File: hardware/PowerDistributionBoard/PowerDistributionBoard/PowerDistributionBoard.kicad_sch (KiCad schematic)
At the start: 17 parts, among them J1 Conn_01x02, Q1 Q_NMOS_GDS, SW1 SW_SPST, U1 LT1641-1

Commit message: Fan Control
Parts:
- added C5, C7: 0.1u, symbol Device:C_Small
- added C6, C8: 2.2n, symbol Device:C_Small
- added J2: FAN 1, symbol Connector_Generic:Conn_01x03
- added J3: FAN 3, symbol Connector_Generic:Conn_01x03
- added J3: FAN 2, symbol Connector_Generic:Conn_01x03
- added J4: FAN 4, symbol Connector_Generic:Conn_01x03
- added Q2, Q5: Q_NPN_EBC, symbol Device:Q_NPN_EBC
- added Q3, Q4, Q6, Q7: Q_NMOS_GSD, symbol Device:Q_NMOS_GSD
- added R10, R11, R12, R13, R8, R9: 4.7k, symbol Device:R_US
- added U2, U3: MAX6643LBBAEET, SOP63P602X175-16N, symbol PBD_LIB:MAX6643LBBAEET
- added U4: MC74HC20ADG, symbol PBD_LIB:MC74HC20ADG
- gave numbers to parts that had none: 1
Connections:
- net GND: now also C5.1, C6.2, C7.1, C8.2, Q2.1 (E), Q3.2 (S), Q4.2 (S), Q5.1 (E), Q6.2 (S), Q7.2 (S), U2.13 (OT2), U2.3 (TL1), U2.7 (GND), U3.13 (OT2), U3.3 (TL1), U3.7 (GND), U4.10 (B2), U4.12 (C2), U4.13 (D2), U4.7 (GND), U4.9 (A2)
- new net: Q3.1 (G), Q4.1 (G), R8.2, U2.12 (PWM_OUT)
- new net: J2.1 (Pin_1), Q3.3 (D)
- new net: C6.1, Q2.2 (B), Q2.3 (C), U2.8 (DXP)
- new net: C8.1, Q5.2 (B), Q5.3 (C), U3.8 (DXP)
- new net: J3.1 (Pin_1), Q6.3 (D)
- new net: Q6.1 (G), Q7.1 (G), R11.2, U3.12 (PWM_OUT)
- new net: J4.1 (Pin_1), Q7.3 (D)
- new net: J3.1 (Pin_1), Q4.3 (D)
- new net +12V: J2.2 (Pin_2), J3.2 (Pin_2), J3.2 (Pin_2), J4.2 (Pin_2)
- new net +3.3V: C5.2, C7.2, R10.1, R11.1, R12.1, R13.1, R8.1, R9.1, U2.14 (OT1), U2.16 (VDD), U2.5 (TACHSET), U3.14 (OT1), U3.16 (VDD), U3.5 (TACHSET), U4.14 (VCC)
- new net FAN_FAIL1: R10.2, U2.4 (~{FANFAIL}), U4.1 (A1)
- new net FAN_FAIL2: R13.2, U3.4 (~{FANFAIL}), U4.4 (C1)
- new net FAN_FULLSPD: U2.6 (FULLSPD), U3.6 (FULLSPD), U4.6 (Y1)
- new net FAN_TACH1: J2.3 (Pin_3), U2.11 (FAN_IN1)
- new net FAN_TACH2: J3.3 (Pin_3), U2.10 (FAN_IN2)
- new net FAN_TACH3: J3.3 (Pin_3), U3.11 (FAN_IN1)
- new net FAN_TACH4: J4.3 (Pin_3), U3.10 (FAN_IN2)
- new net OVERTEMP1: R9.2, U2.9 (~{OT}), U4.2 (B1)
- new net OVERTEMP2: R12.2, U3.9 (~{OT}), U4.5 (D1)
- no-connect marks 0 -> 9
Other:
- note added: "T_HIGH=40C T_LOW=30C T_OVERTEMP=70C"

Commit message: Add 12V DC-DC and Estop Relays
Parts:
- added C10: 10uF, symbol Device:C_Polarized_US
- added C11: 1uF, symbol Device:C_Small
- added C9: 33u, symbol Device:C_Polarized_US
- added D? (x2): D, symbol Device:D
- added F1: 1A, symbol Device:Fuse
- added J6: Inverter, symbol Connector_Generic:Conn_01x02
- added J7: Control Board, symbol Connector_Generic:Conn_01x02
- added J?: ESC1_PWR, symbol Connector_Generic:Conn_01x02
- added J?: Conn_01x02, symbol Connector_Generic:Conn_01x02
- added J?: ESC2_PWR, symbol Connector_Generic:Conn_01x02
- added K1, K2: J115F11AH12VDCS61.5, symbol PBD_LIB:J115F11AH12VDCS61.5
- added Q8: Q_NPN_BCE, symbol Device:Q_NPN_BCE
- added Q?: Q_NMOS_GDS, symbol Device:Q_NMOS_GDS
- added R14: 0, symbol Device:R_US
- added R15, R16: DNP, symbol Device:R_US
- added R?: R_US, symbol Device:R_US
- added U5: KSTW004A2B41Z, symbol PBD_LIB:KSTW004A2B41Z
- J1: value Conn_01x02 -> Battery
- renumbered J3 to J4, J4 to J5
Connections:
- net +12V: now also C10.1, C11.1, D?.1 (K), D?.1 (K), J7.1 (Pin_1), K1.2, K2.2, R15.1, U5.7 (SENSE+), U5.8 (VO+)
- net +48V: now also F1.1, J6.1 (Pin_1), K1.5, K2.5
- net GND: now also C10.2, C11.2, C9.2, J6.2 (Pin_2), J7.2 (Pin_2), J?.2 (Pin_2), J?.2 (Pin_2), J?.2 (Pin_2), Q8.3 (E), R14.2, R16.2, U5.3 (VIN-), U5.4 (VO-), U5.5 (SENSE-)
- new net: D?.2 (A), D?.2 (A), K1.1, K2.1, Q8.2 (C)
- new net: R15.2, R16.1, U5.6 (TRIM)
- new net: C9.1, F1.2, U5.1 (VIN+)
- new net: R14.1, U5.2 (ON/OFF)
- new net: Q8.1 (B), R?.1
- new net ESC1_PWR: J?.1 (Pin_1), K1.3
- new net ESC2_PWR: J?.1 (Pin_1), K2.3
- new net ESTOP: J?.1 (Pin_1), R?.2
- no-connect marks 9 -> 11
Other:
- note added: "12V CONVERTER"
- note added: "50W"
- note added: "C10 tantalum"
- note added: "C9 electrolytic"
- note added: "ESC RELAYS"
- note added: "FANS"
- note added: "Need snubber across contacts??"
- note added: "POWER INTAKE"
- note added: "POWER OUTPUT CONNECTORS"
- note added: "coil current for each relay will be ~125mA IC for Q8 is 250mA Worst case current gain is 40 @ VCE=10V, IC=500mA Gives IB=IC/hFE=250/40=6.25mA RB=(VIO-VBE)/IB VBE=0.6V min or 1.2V max @ IC=150mA, or 2.0V max @ IC=500mA Check VIO of whatever is gonna drive ESTOP signal"
- moved on the sheet: C1, C2, C3, C4, C5, C6, C7, C8, D1, J1, J2, J3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

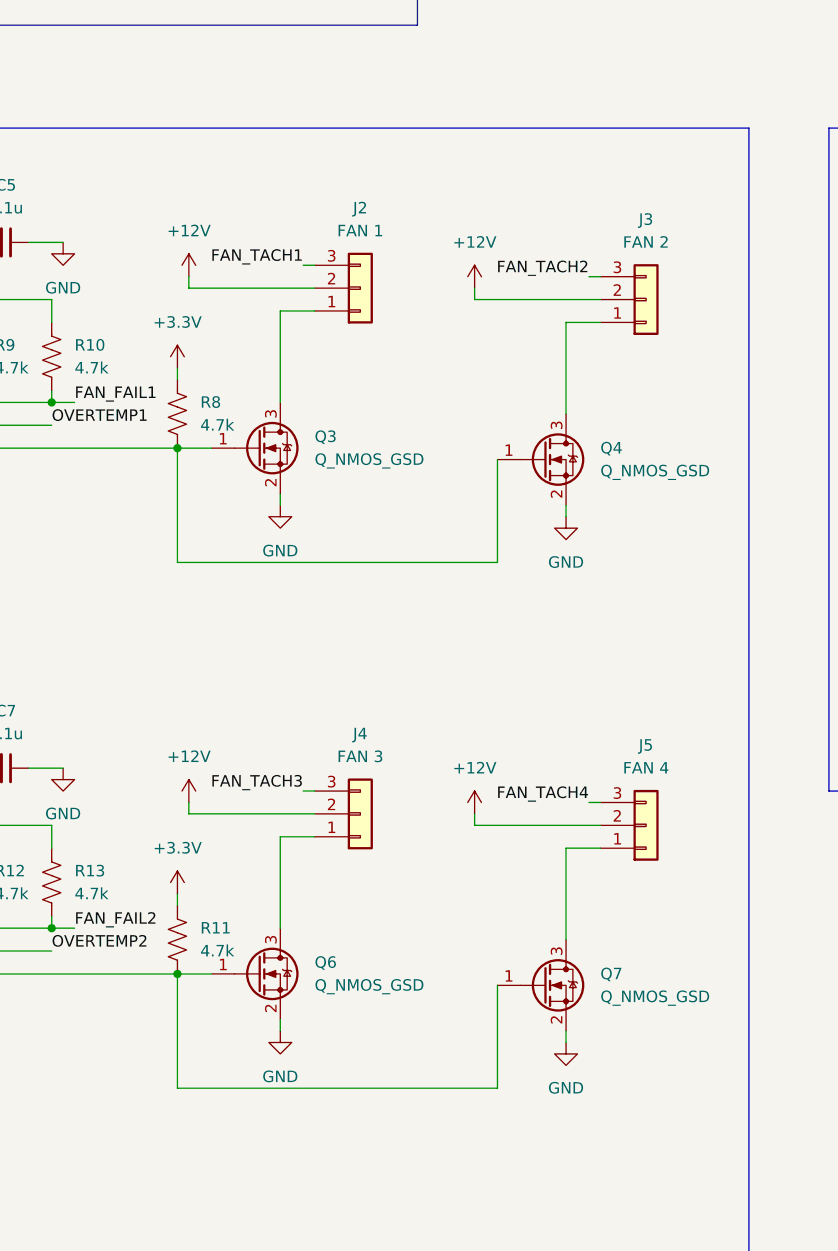
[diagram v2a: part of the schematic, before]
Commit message: Added Resistor Options on Fans
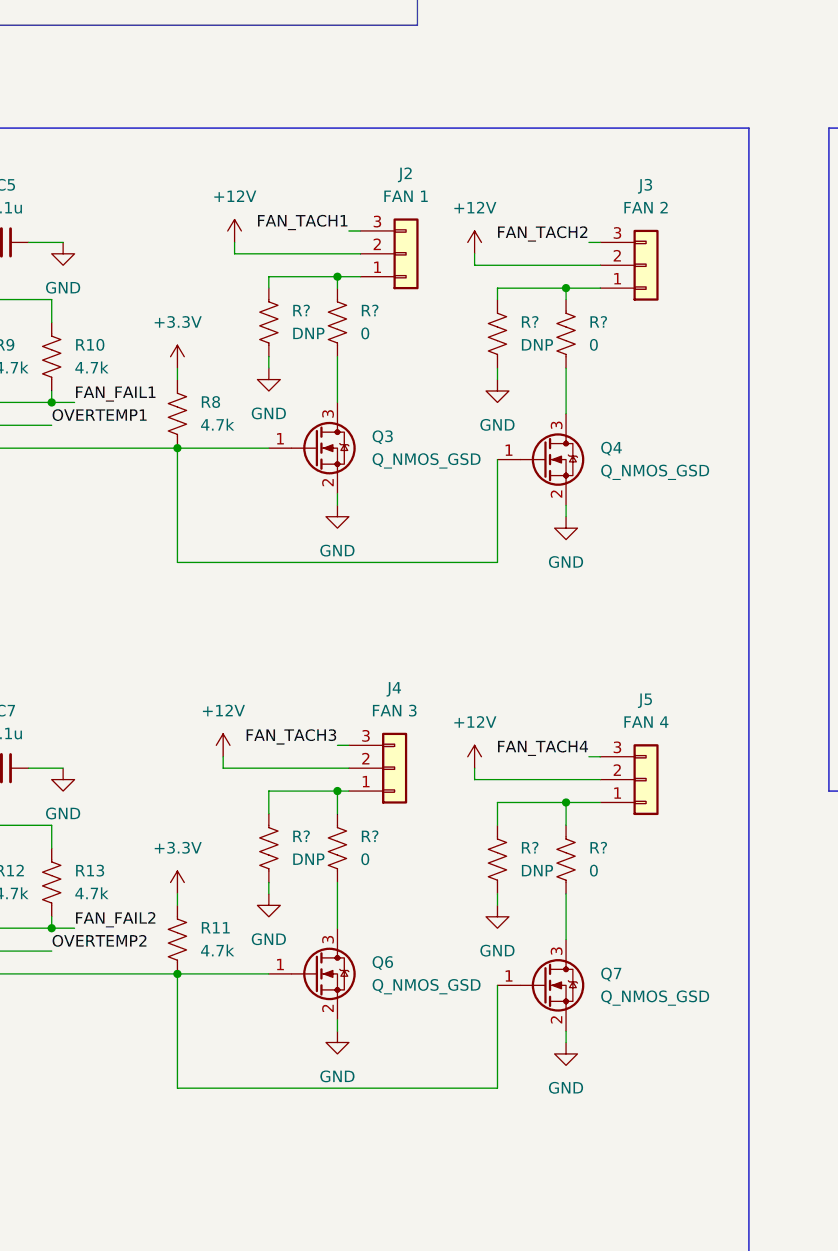
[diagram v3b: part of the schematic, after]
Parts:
- added R? (x4): DNP, symbol Device:R_US
- added R? (x4): 0, symbol Device:R_US
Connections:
- net GND: now also R?.2, R?.2, R?.2, R?.2
- net at Q3.3 (D): now also R?.2; no longer J2.1 (Pin_1)
- net at J4.1 (Pin_1): now also R?.1, R?.1; no longer Q6.3 (D)
- net at Q7.3 (D): now also R?.2; no longer J5.1 (Pin_1)
- net at J3.1 (Pin_1): now also R?.1, R?.1; no longer Q4.3 (D)
- new net: J2.1 (Pin_1), R?.1, R?.1
- new net: Q6.3 (D), R?.2
- new net: Q4.3 (D), R?.2
- new net: J5.1 (Pin_1), R?.1, R?.1
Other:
- moved on the sheet: J2, J3, J4, J5, Q3, Q6

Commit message: Add 3v3 LDO and Some Test Points
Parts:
- added C?: 1u, symbol Device:C_Small
- added C?: 2.2u, symbol Device:C_Small
- added TP? (x4): TestPoint, symbol Connector:TestPoint
- added U?: AP2210N-3.3TRG1, symbol PBD_LIB:AP2210N-3.3TRG1
- C4: value BULK -> 1000u
- R1: value 68k -> 43k
- R2: value 2.2k -> 1.3k
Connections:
- net +12V: now also C?.1, TP?.1, U?.3 (VI)
- net +3.3V: now also C?.1, TP?.1, U?.2 (VO)
- net ESTOP: now also TP?.1
- net GND: now also C?.2, C?.2, U?.1 (GND)
- net at R1.2, R2.1, SW1.2 (B)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: now also TP?.1
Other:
- note added: "3V3 LDO"
- note added: "Could add resistor options for temp settings but 2 options (no R for NC) x 6 pins x 2 parts is 24 resistors maybe add GND and VCC pads near parts to hook onto in worst case"
- note added: "This is a guess"
- note added: "UVLO Trip at 42V Restart at 44.7V"
- note removed: "UVLO Trip at 39.3V Restart at 42V"
- moved on the sheet: C10, J6, J7, J?, R?, SW1

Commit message: Small stuff
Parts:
- removed Q?: Q_NMOS_GDS, symbol Device:Q_NMOS_GDS
- added C?: 0.1u, symbol Device:C_Small
- added D? (x2): D, symbol Device:D
- C1: value 6.8n -> 0.68u
- R4: value 0.6m -> 0.75m
- U6: renamed from U?; Digikey (none) -> AP2210N-3.3TRG1DICT-ND
- gave numbers to parts that had none: 20
- renumbered R8 to R26
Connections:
- net ESC1_PWR: now also D?.1 (K)
- net ESC2_PWR: now also D?.1 (K)
- net GND: now also C?.2, D?.2 (A), D?.2 (A)
- net at R1.2, R2.1, SW1.2 (B)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: now also C?.1
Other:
- note added: "C1 gives ~11ms current limit time Too long?"
- note added: "Going off 800W max for motors"
- note added: "R4 is sense resistor Vsense=47mV 0.75mohm gives 62.67A limit (~3kW at 48V) R4 dissipates 2.95W at max I May have to swap this out depending on battery limit"
- note added: "REVIEW V0.1"
- note removed: "C1 gives 0.1ms current limit time"
- note removed: "Vsense=47mV 0.6mohm gives 78.33A limit 3.68W at max I"
- moved on the sheet: C2, J10, J9, SW1, TP1

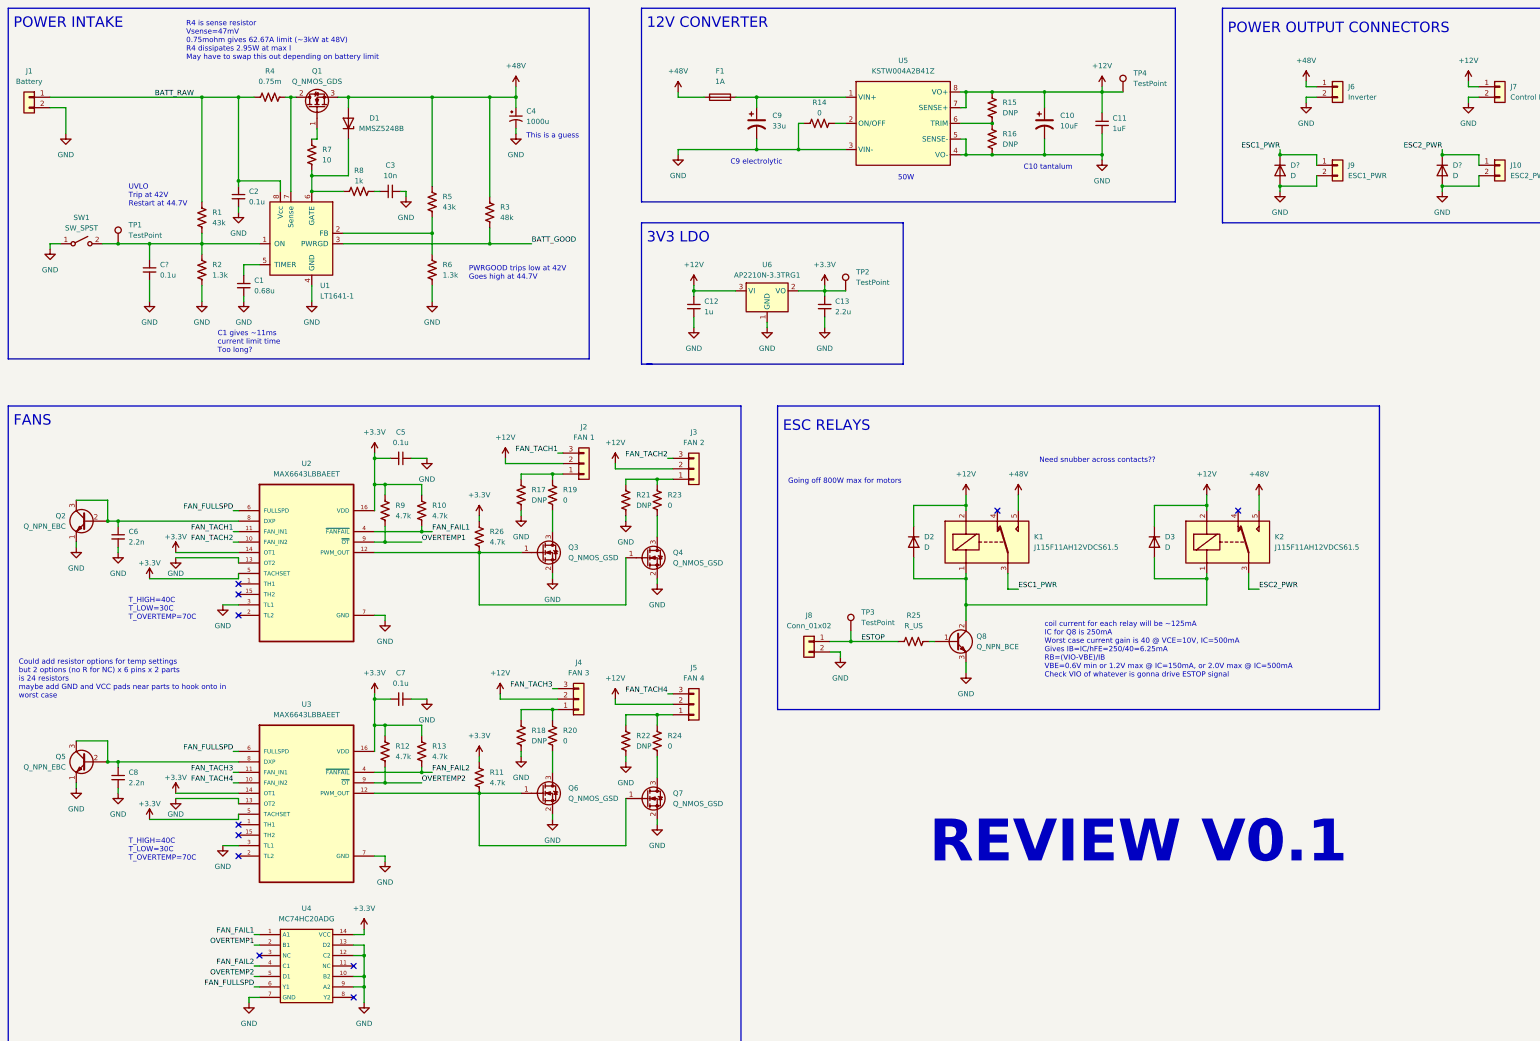
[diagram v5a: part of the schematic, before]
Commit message: Add footprints and start layout on PDB, start control board schematic
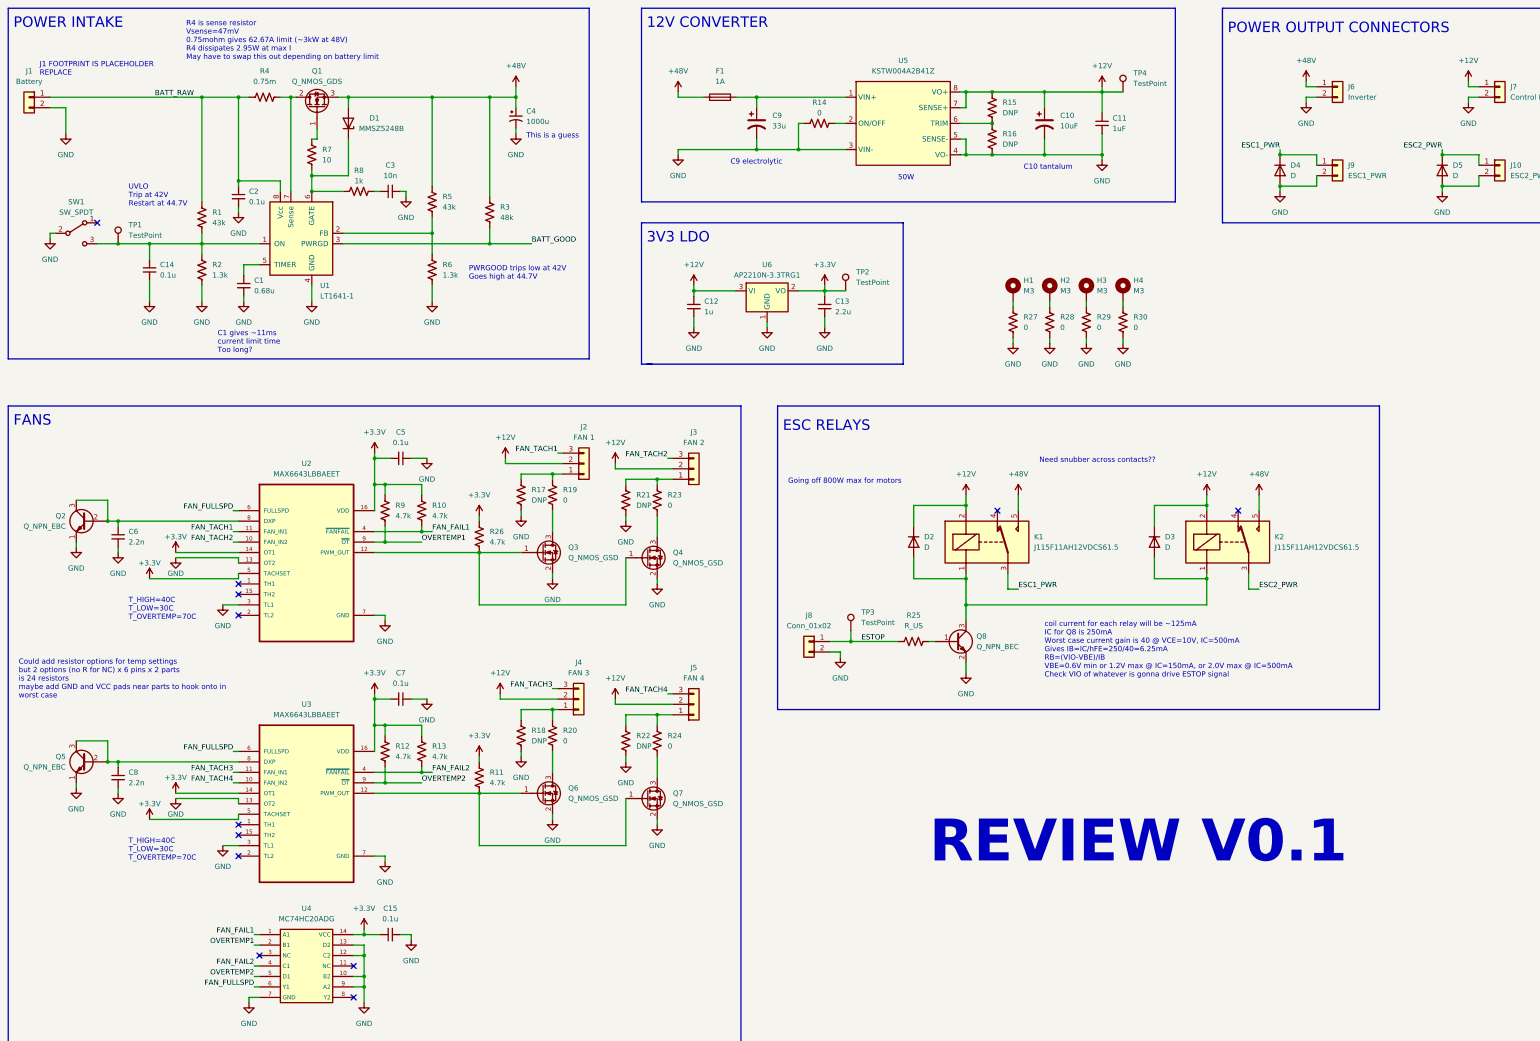
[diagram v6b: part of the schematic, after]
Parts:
- removed Q8: Q_NPN_BCE, symbol Device:Q_NPN_BCE
- removed SW1: SW_SPST, symbol Switch:SW_SPST
- added C15: 0.1u, Capacitor_SMD:C_0805_2012Metric, symbol Device:C_Small
- added H1, H2, H3, H4: M3, MountingHole:MountingHole_3.2mm_M3_Pad_Via, symbol Mechanical:MountingHole_Pad
- added Q8: Q_NPN_BEC, Package_TO_SOT_SMD:SOT-23, symbol Device:Q_NPN_BEC
- added R27, R28, R29, R30: 0, Resistor_SMD:R_0805_2012Metric, symbol Device:R_US
- added SW1: SW_SPDT, PDBLib:EG1218, symbol Switch:SW_SPDT
- C1, C11, C12, C13, C2, C3, C5, C6, C7, C8: footprint (none) -> Capacitor_SMD:C_0805_2012Metric
- C10: footprint (none) -> Capacitor_SMD:C_1206_3216Metric; Digikey (none) -> 478-10001-1-ND
- C14: renamed from C?; footprint (none) -> Capacitor_SMD:C_0805_2012Metric
- C4: footprint (none) -> Capacitor_THT:CP_Radial_D18.0mm_P7.50mm; Digikey (none) -> 493-1152-ND
- C9: footprint (none) -> Capacitor_THT:CP_Radial_D12.5mm_P5.00mm; Digikey (none) -> 4191-PF2D330MCE1212F3-ND
- D1: footprint (none) -> Diode_SMD:D_SOD-123
- D2, D3: footprint (none) -> Diode_SMD:D_SMA
- D4, D5: renamed from D?; footprint (none) -> Package_TO_SOT_THT:TO-247-2_Horizontal_TabDown
- F1: footprint (none) -> PDBLib:0679L1000-05
- J1: footprint (none) -> Connector_Molex:Molex_Mini-Fit_Sr_42820-22XX_1x02_P10.00mm_Horizontal
- J10, J6, J9: footprint (none) -> Connector_Molex:Molex_Mini-Fit_Sr_42820-22XX_1x02_P10.00mm_Horizontal; Digikey (none) -> WM11250-ND
- J2, J3, J4, J5: footprint (none) -> Connector_Molex:Molex_KK-254_AE-6410-03A_1x03_P2.54mm_Vertical; Digikey (none) -> WM4112-ND
- J7, J8: footprint (none) -> Connector_Molex:Molex_Micro-Fit_3.0_43650-0200_1x02_P3.00mm_Horizontal; Digikey (none) -> WM1860-ND
- K1, K2: footprint (none) -> PDBLib:J115F11AH12VDCS61.5; Digikey (none) -> 2449-J115F11AH12VDCS61.5-ND
- Q1: footprint (none) -> Package_TO_SOT_SMD:TO-263-3_TabPin2
- Q2, Q5: footprint (none) -> PDBLib:SST3904T116CT-ND
- Q3, Q4, Q6, Q7: footprint (none) -> Package_TO_SOT_SMD:SC-59
- R1, R10, R11, R12, R13, R14, R15, R16, R17, R18, R19, R2, R20, R21, R22, R23, R24, R25, R26, R3, R5, R6, R7, R8, R9: footprint (none) -> Resistor_SMD:R_0805_2012Metric
- R4: footprint (none) -> PDBLib:Y14860R00075F9R; Digikey (none) -> 804-Y14860R00075F9RCT-ND
- TP1, TP2, TP3, TP4: footprint (none) -> TestPoint:TestPoint_Pad_D1.0mm
- U2, U3: footprint SOP63P602X175-16N -> Package_SO:QSOP-16_3.9x4.9mm_P0.635mm
- U4: footprint (none) -> Package_SO:SOIC-14_3.9x8.7mm_P1.27mm
- U5: footprint (none) -> PDBLib:CONV_KSTW004A2B41Z
- U6: footprint (none) -> PDBLib:AP2210N-3.3TRG1
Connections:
- net +3.3V: now also C15.1
- net GND: now also C15.2, Q8.2 (E), R27.2, R28.2, R29.2, R30.2, SW1.2 (B)
- net at C14.1, R1.2, R2.1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: now also SW1.3 (C)
- net at D2.2 (A), D3.2 (A), K1.1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: now also Q8.3 (C)
- net at R25.1: now also Q8.1 (B)
- new net: H4.1, R30.1
- new net: H1.1, R27.1
- new net: H2.1, R28.1
- new net: H3.1, R29.1
- no-connect marks 11 -> 12
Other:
- note added: "J1 FOOTPRINT IS PLACEHOLDER REPLACE"
- moved on the sheet: R4

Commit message: PDB Routing First Pass
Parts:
- added C16: 0.1u, Capacitor_SMD:C_0805_2012Metric, symbol Device:C_Small
- added C17: 33u, Capacitor_THT:CP_Radial_D12.5mm_P5.00mm, symbol Device:C_Polarized_US
- added D6, D7: Green, LED_SMD:LED_0805_2012Metric_Pad1.15x1.40mm_HandSolder, symbol Device:LED
- added R31: 700, Resistor_SMD:R_0805_2012Metric, symbol Device:R_US
- added R32: 5.1k, Resistor_SMD:R_0805_2012Metric, symbol Device:R_US
- added R33: 3k, Resistor_SMD:R_0805_2012Metric, symbol Device:R_US
- J8: footprint Connector_Molex:Molex_Micro-Fit_3.0_43650-0200_1x02_P3.00mm_Horizontal -> Connector_Molex:Molex_Micro-Fit_3.0_43650-0215_1x02_P3.00mm_Vertical; Digikey WM1860-ND -> WM1917-ND
- R25: value R_US -> 360
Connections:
- net +12V: now also R32.1
- net +3.3V: now also R31.2
- net +48V: now also C17.1
- net ESTOP: now also C16.1, R33.1; no longer J8.1 (Pin_1)
- net GND: now also C16.2, C17.2, D6.1 (K), D7.1 (K)
- new net: D7.2 (A), R32.2
- new net: J8.1 (Pin_1), R33.2
- new net: D6.2 (A), R31.1
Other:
- moved on the sheet: C1, C14, C2, C3, C4, D1, D2, D3, D4, D5, J1, J10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
